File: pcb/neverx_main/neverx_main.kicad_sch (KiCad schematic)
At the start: 18 parts, among them J1 DB1, J2 DB1, J3 DB1, J4 DB1, J5 DB1, J6 DB1, SW1 VAL, SW2 CONF, U1 LilyGO_T-SIM7080G-S3, U3 IPS_240_240

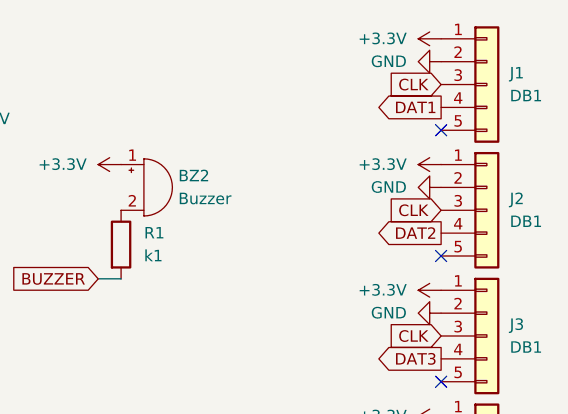
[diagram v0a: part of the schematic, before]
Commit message: Fixed wrongtraces
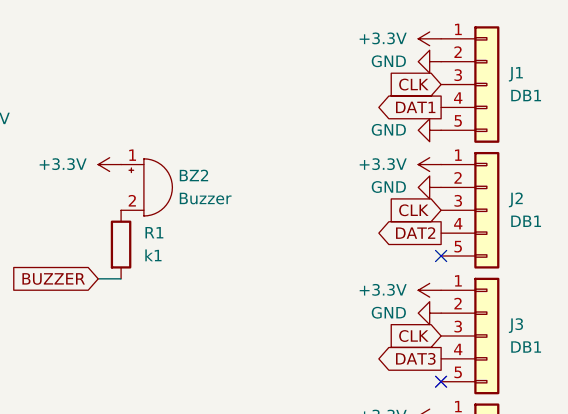
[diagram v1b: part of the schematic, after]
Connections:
- net GND: now also J1.5 (Pin_5)
- no-connect marks 6 -> 5
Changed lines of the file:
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@@
-	)
-	(no_connect
-		(at 173.99 40.64)
 	)
 	(no_connect
@@
 					(unit 1)
 				)
+			)
+		)
+	)
+	(symbol
+		(lib_id "power:GND")
+		(at 173.99 40.64 270)
+		(unit 1)
+		(exclude_from_sim no)
+		(in_bom yes)
+		(on_board yes)
+		(dnp no)
+		(fields_autoplaced yes)
+		(property "Reference" "#PWR021"
+			(at 167.64 40.64 0)
+			(effects
+				(font
+					(size 1.27 1.27)
+				)
+				(hide yes)
+			)
+		)
+		(property "Value" "GND"
+			(at 170.18 40.6399 90)
+			(effects
+				(font
+					(size 1.27 1.27)
+				)
+				(justify right)
+			)
+		)
+		(property "Footprint" ""
+			(at 173.99 40.64 0)
+			(effects
+				(font
+					(size 1.27 1.27)
+				)
+				(hide yes)
+			)
+		)
+		(property "Datasheet" ""
+			(at 173.99 40.64 0)
+			(effects
+				(font
+					(size 1.27 1.27)
+				)
+				(hide yes)
+			)
+		)
+		(property "Description" "Power symbol creates a global label with name \"GND\" , ground"
+			(at 173.99 40.64 0)
+			(effects
+				(font
+					(size 1.27 1.27)
+				)
+				(hide yes)
+			)
+		)
+		(pin "1"
+		)
+		(instances
+			(project "neverx_main"
+				(path "/6675e5df-9247-450e-a1aa-9f608398aef1"
+					(reference "#PWR021")
+					(unit 1)
+				)
